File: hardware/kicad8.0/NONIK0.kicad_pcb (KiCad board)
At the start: 2 copper layers, 55 x 22 mm, 25 parts, among them J1 AVR-UPDI-3, J2 Qwiic/Stemma QT, J3 Test Pads, J4 Test Pads, SW1 SW_SPST, SW2 SW_Push, SW3 SW_Push, U1 LED_HCMS-2915, U2 ATtiny1604-SS, U3 AP3602A

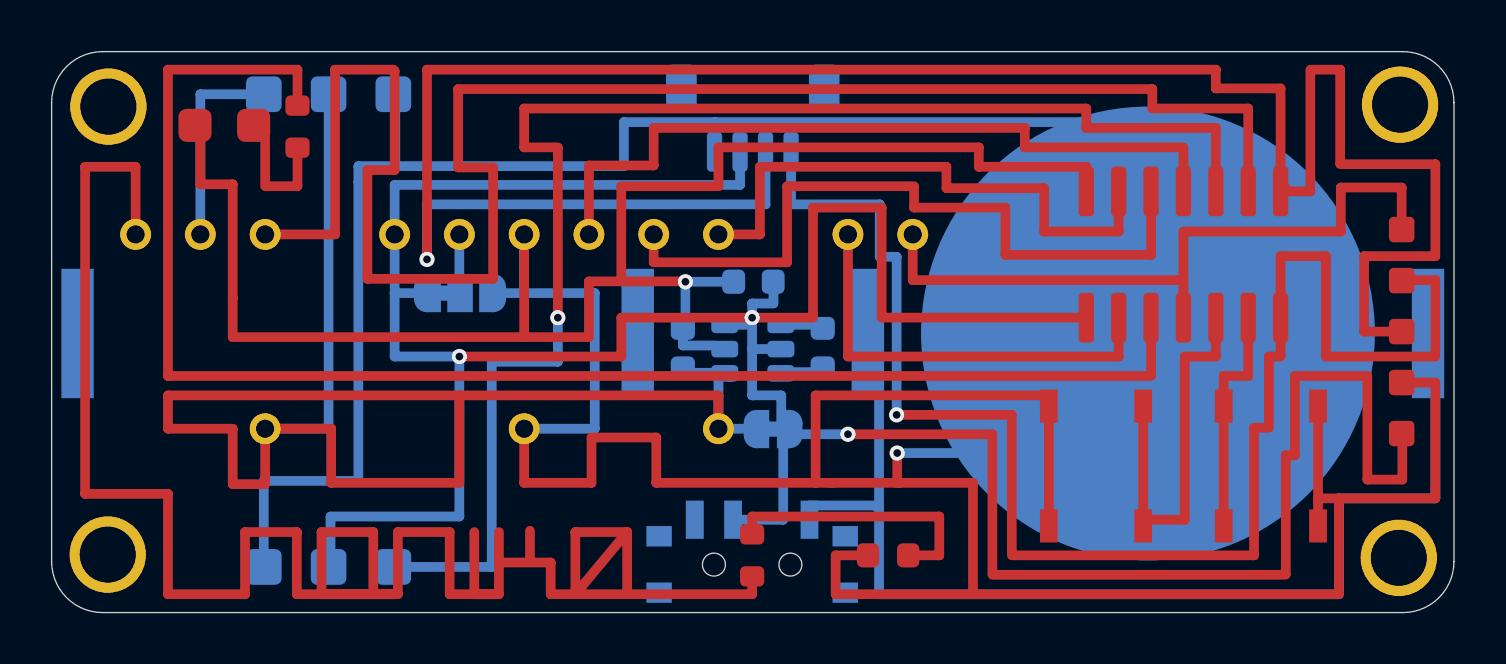
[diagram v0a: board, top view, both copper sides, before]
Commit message: adding bjt to drive buzzer
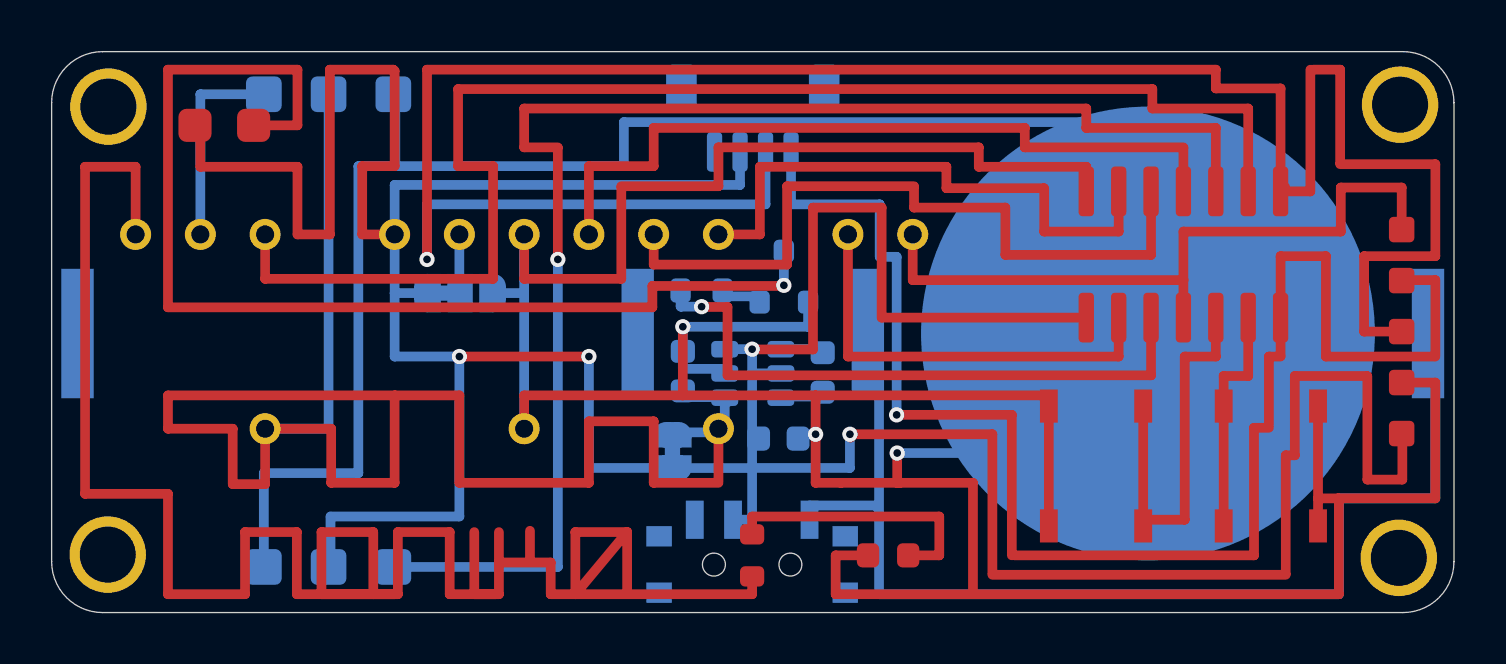
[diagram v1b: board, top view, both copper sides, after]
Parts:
- added Q1: S8050, NONIK0:SOT-23-SmallerCourtyard, B.Cu at (71.6, 26.5)
- JP2: footprint Jumper:SolderJumper-3_P1.3mm_Bridged12_RoundedPad1.0x1.5mm -> NONIK0:SolderJumper-3_P1.3mm_Bridged12_RoundedPad1.0x1.5mm
- R2: value 1K -> 180; moved to B.Cu
- moved R2 17.1 mm to (68.4, 27.0), turned to 180 degrees
- moved C1 6.23 mm to (71.4, 32.8), turned to 180 degrees
- moved JP1 4.04 mm to (67.2, 33.3), turned to -90 degrees
- moved C2 0.96 mm to (73.1, 30.2)
- moved U3 0.96 mm to (70.4, 30.3)
- moved C3 0.90 mm to (67.6, 30.2)
- turned BZ1 to 90 degrees
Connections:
- BZ1 pad 1: Net-(BZ1-+) -> VCC
- BZ1 pad 2: GND -> Net-(BZ1--)
- R2 pad 1: Net-(BZ1-+) -> Net-(Q1-B)
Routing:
- net Net-(BZ1--): track 0.00 -> 44.7 mm, vias 0 -> 1
- net BUZZ: track 59.3 -> 23.6 mm, vias 0 -> 1
- net GND: track 260.8 -> 230.8 mm, vias 2 -> 3
- net VCC: track 133.9 -> 162.3 mm, vias 3 -> 4
- net RESET: track 69.6 -> 54.5 mm
- net Vled: track 66.6 -> 73.0 mm
- net Net-(BZ1-+): track 4.62 -> 0.00 mm
- net Net-(Q1-B): track 0.00 -> 1.45 mm

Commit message: fit and finish
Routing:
- net VCC: track 162.3 -> 161.3 mm

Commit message: pcb fixes, in progress
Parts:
- moved JP2 0.40 mm to (58.9, 27.5)
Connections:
- U2 pad 7: SCL -> RESET
- U2 pad 9: RESET -> SCL
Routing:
- net VCC: track 161.3 -> 143.7 mm, vias 4 -> 5
- net RESET: track 54.4 -> 67.1 mm
- net SCL: track 61.5 -> 73.5 mm
- net GND: track 230.7 -> 221.9 mm, vias 3 -> 5
- net CE: track 28.9 -> 24.6 mm
- net Net-(Q1-B): track 1.45 -> 4.82 mm
- net Vled: track 73.0 -> 71.7 mm
- net Net-(BZ1--): track 44.8 -> 44.1 mm

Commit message: pcb fixes
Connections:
- J3 pad 1: DIN -> SCL
- J3 pad 2: SCL -> DIN
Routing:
- net Vled: track 71.7 -> 65.9 mm
- net DIN: track 28.0 -> 32.3 mm
- net SCL: track 73.5 -> 69.9 mm
- net RS: track 17.0 -> 13.8 mm
- net Net-(BZ1--): track 44.1 -> 46.5 mm
- net GND: track 221.9 -> 219.9 mm, vias 5 -> 7
- net BUZZ: track 23.7 -> 22.1 mm
- net CLK: track 22.8 -> 21.2 mm
- net RESET: track 67.1 -> 66.3 mm
- net VCC: track 143.7 -> 144.4 mm

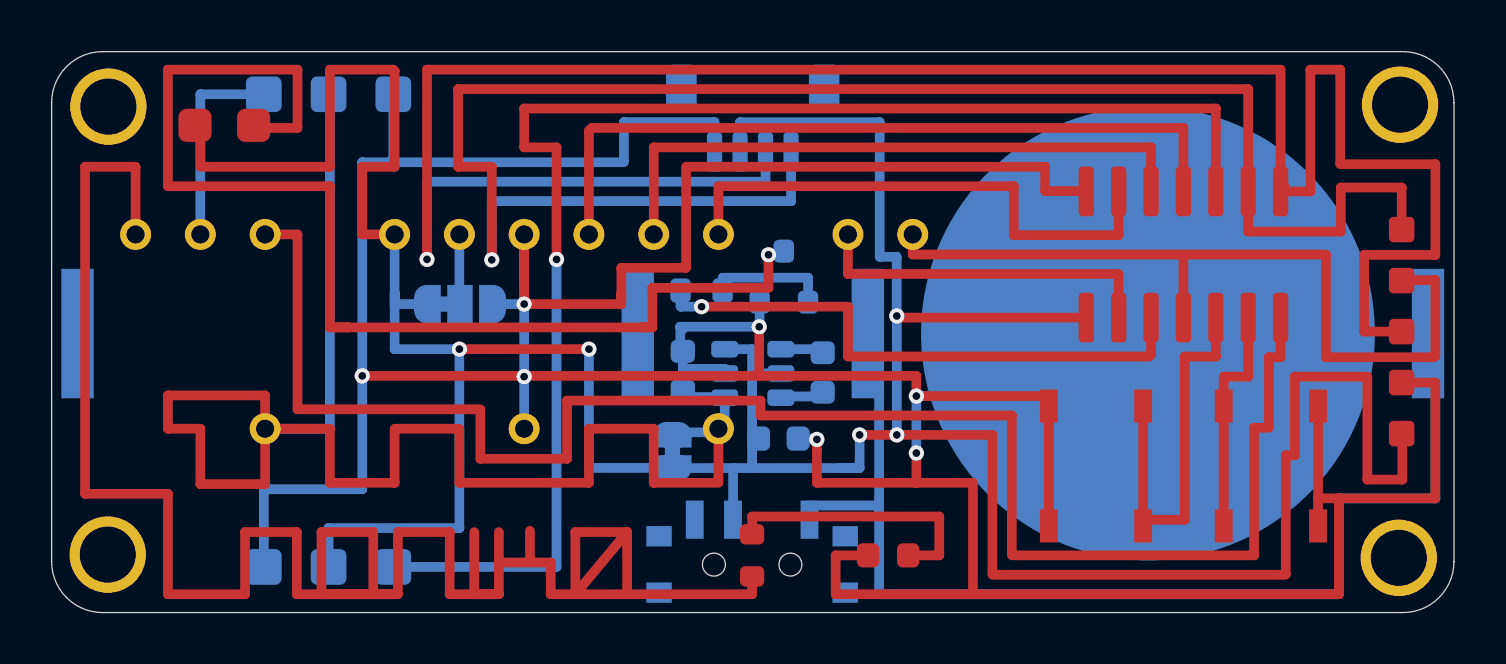
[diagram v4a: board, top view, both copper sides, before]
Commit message: adding flyback diode
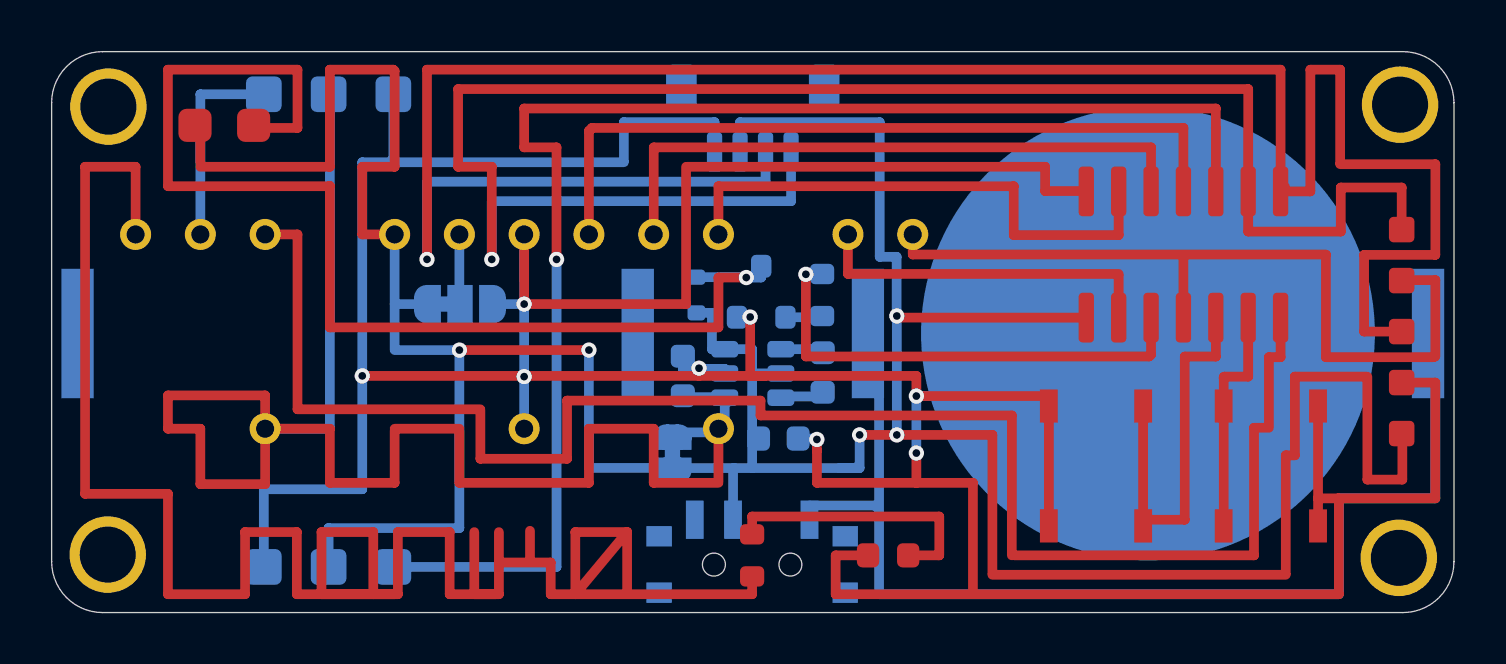
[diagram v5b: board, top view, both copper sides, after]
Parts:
- added D2: 1N4148WT, NONIK0:D_SOD-523_NoSilkscreen, B.Cu at (68.2, 27.2)
- JP1: footprint NONIK0:SolderJumper-2_P1.3mm_Bridged_RoundedPad1.0x1.5mm -> NONIK0:SolderJumper_SmallerFootprint
- U3: footprint NONIK0:SOT-23-6 -> NONIK0:SOT-23-6_SmallerFootprint
- moved R2 4.73 mm to (73.1, 27.2), turned to 90 degrees
- moved Q1 1.07 mm to (70.7, 27.1)
- moved C3 0.19 mm to (67.6, 30.4)
- moved JP1 0.09 mm to (67.2, 33.4)
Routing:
- net GND: track 219.9 -> 216.3 mm, vias 7 -> 8
- net Net-(Q1-B): track 4.82 -> 1.49 mm
- net BUZZ: track 22.1 -> 18.9 mm
- net VCC: track 144.4 -> 146.5 mm
- net Net-(BZ1--): track 46.5 -> 47.9 mm
